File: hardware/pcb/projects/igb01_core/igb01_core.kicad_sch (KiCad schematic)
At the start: 65 parts, among them J1 STMP157_GPIO1, J10 BAT_CON, J11 VBUS_CON, J12 IGB2_NEXT, J13 IGB3_NEXT, J14 IGB4_NEXT, J15 I2C_PREV, J16 I2C_NEXT, J17 JTAG, J18 USB, J19 PWR_ON_CON, J2 STMP157_GPIO3, J20 FPA-VZA2-15-LF, J21 I2C2_NEXT, J3 STMP157_GPIO2, J4 STMP157_GPIO4, J5 STMP157_GPIO5, J6 STMP157_GPIO6, J7 LEFT_CON, J8 RIGHT_CON, J9 Micro_SD_Card, SW1 SW_DIP_x04, SW2 SW_Push, SW3 SW_Push, U1 W25Q128JVS

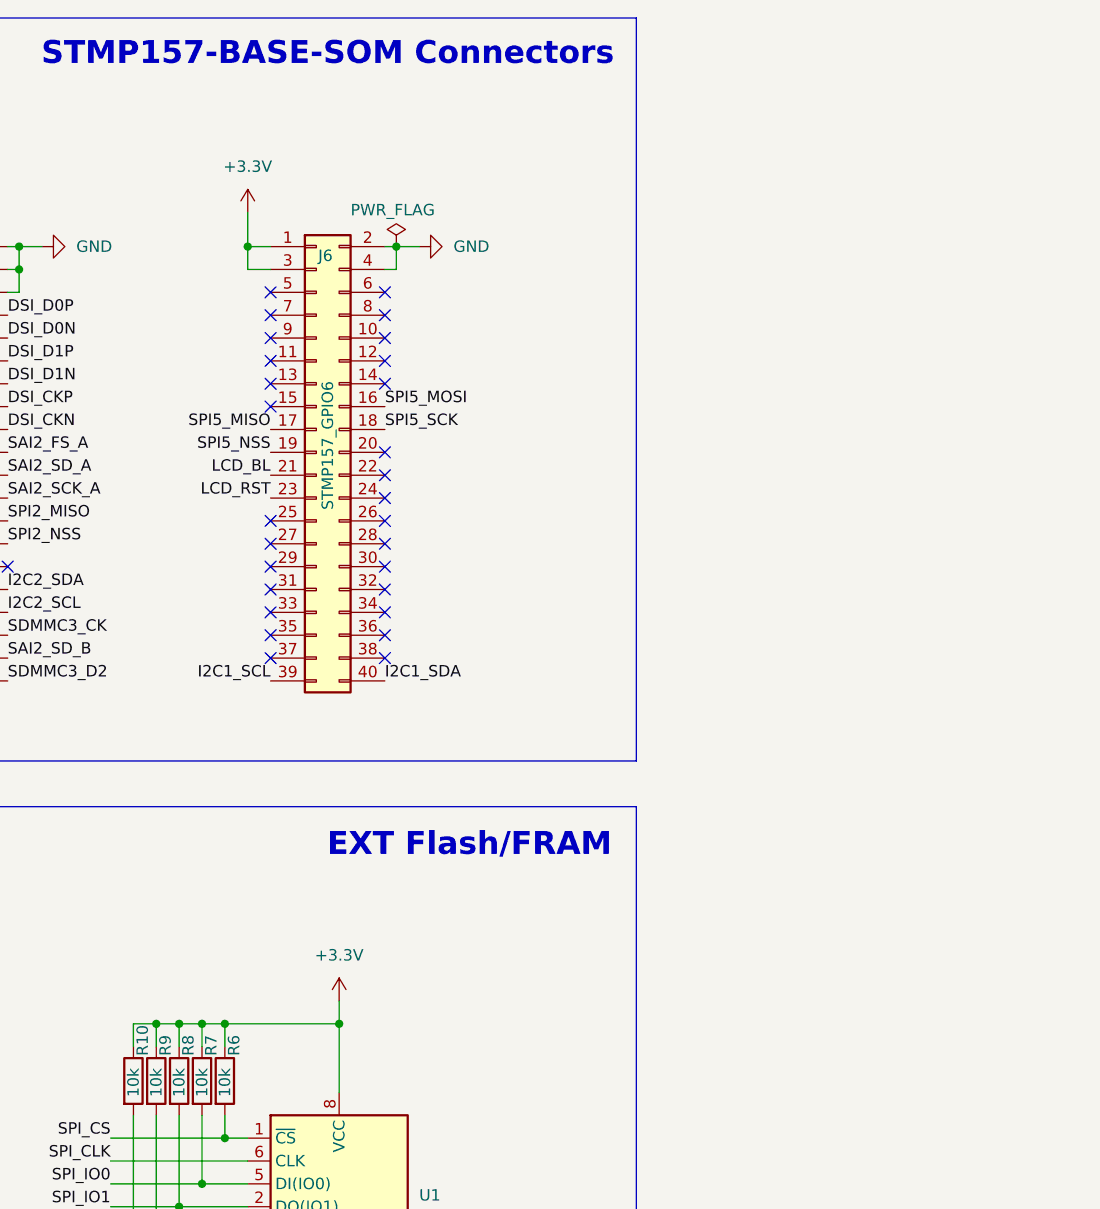
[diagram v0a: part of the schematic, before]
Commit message: add Config pins & Ext GPIO pins
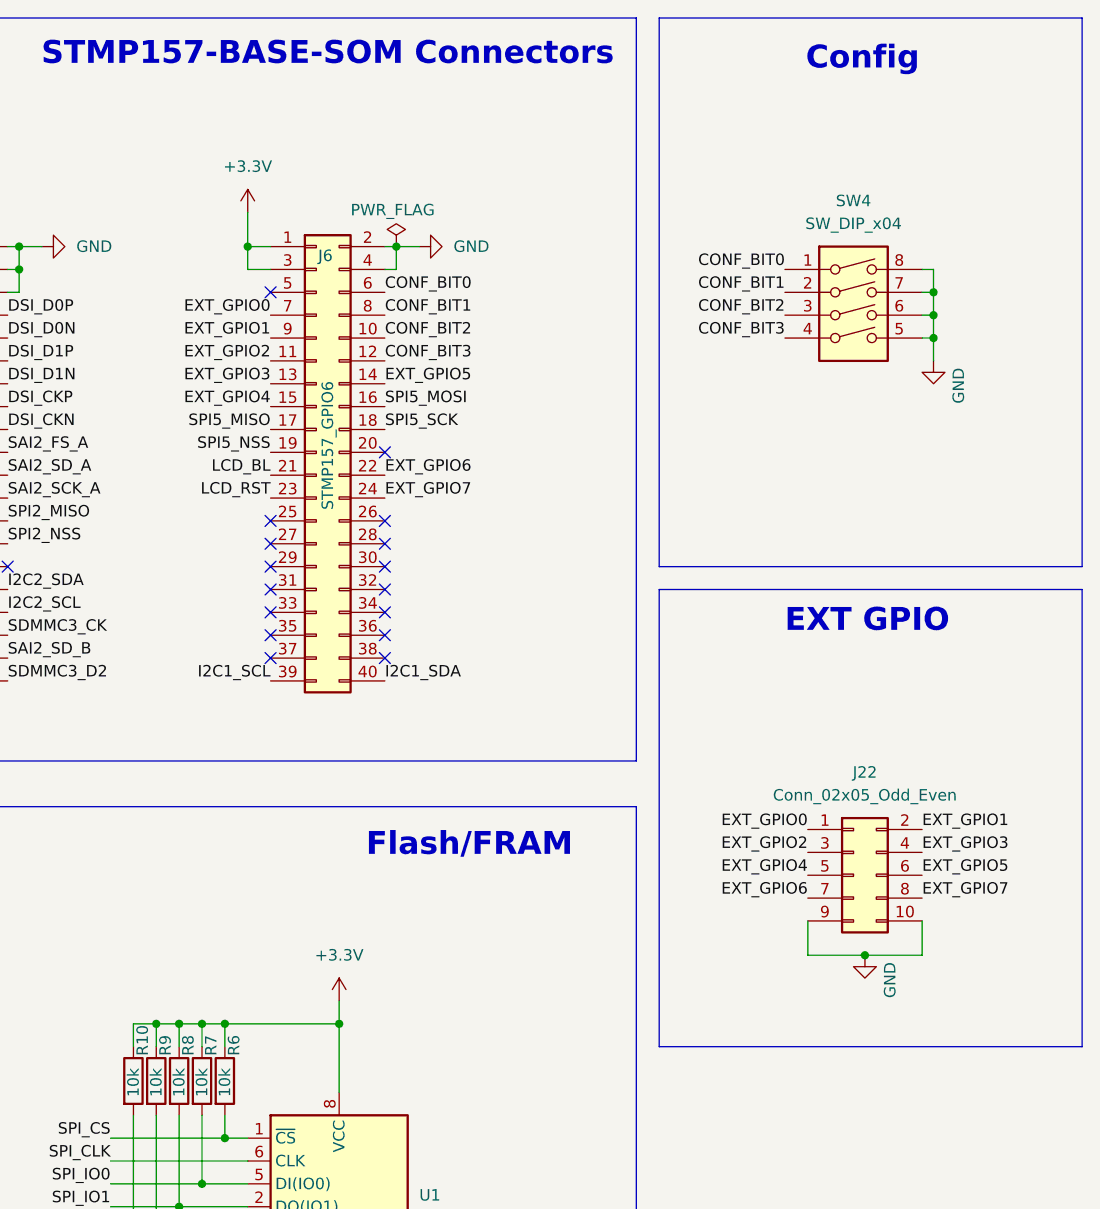
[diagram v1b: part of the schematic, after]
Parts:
- added J22: Conn_02x05_Odd_Even, symbol Connector_Generic:Conn_02x05_Odd_Even
- added SW4: SW_DIP_x04, symbol Switch:SW_DIP_x04
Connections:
- net GND: now also J22.10 (Pin_10), J22.9 (Pin_9), SW4.5, SW4.6, SW4.7, SW4.8
- net CONF_BIT2: now reaches J6.10 (Pin_10)
- net CONF_BIT2: now also SW4.3
- net EXT_GPIO2: now reaches J6.11 (Pin_11)
- net EXT_GPIO2: now also J22.3 (Pin_3)
- net CONF_BIT3: now reaches J6.12 (Pin_12)
- net CONF_BIT3: now also SW4.4
- net EXT_GPIO3: now reaches J6.13 (Pin_13)
- net EXT_GPIO3: now also J22.4 (Pin_4)
- net EXT_GPIO5: now reaches J6.14 (Pin_14)
- net EXT_GPIO5: now also J22.6 (Pin_6)
- net EXT_GPIO4: now reaches J6.15 (Pin_15)
- net EXT_GPIO4: now also J22.5 (Pin_5)
- net EXT_GPIO6: now reaches J6.22 (Pin_22)
- net EXT_GPIO6: now also J22.7 (Pin_7)
- net EXT_GPIO7: now reaches J6.24 (Pin_24)
- net EXT_GPIO7: now also J22.8 (Pin_8)
- net CONF_BIT0: now reaches J6.6 (Pin_6)
- net CONF_BIT0: now also SW4.1
- net EXT_GPIO0: now reaches J6.7 (Pin_7)
- net EXT_GPIO0: now also J22.1 (Pin_1)
- net CONF_BIT1: now reaches J6.8 (Pin_8)
- net CONF_BIT1: now also SW4.2
- net EXT_GPIO1: now reaches J6.9 (Pin_9)
- net EXT_GPIO1: now also J22.2 (Pin_2)
- no-connect marks 133 -> 121
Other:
- note added: "Config"
- note added: "EXT GPIO"
- note added: "Flash/FRAM"
- note removed: "EXT Flash/FRAM"

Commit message: add CODEC_PDN pin & 3.3V Out pin
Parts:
- J7, J8: symbol Connector_Generic:Conn_01x23 -> Connector_Generic:Conn_01x25
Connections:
- net +3.3V: now also J7.3 (Pin_3)
- net ADC1_INP1: now also J8.24 (Pin_24); no longer J7.3 (Pin_3)
- net ADC2_INP18: now also J8.25 (Pin_25); no longer J8.3 (Pin_3)
- net GND: now also J7.4 (Pin_4), J7.5 (Pin_5)
- net GPIO_CLOCK_OUT: now also J8.4 (Pin_4); no longer J8.5 (Pin_5)
- net GPIO_RESET_OUT: now also J8.3 (Pin_3); no longer J8.4 (Pin_4)
- net SDMMC3_CK: now also J7.24 (Pin_24); no longer J7.22 (Pin_22)
- net SDMMC3_CMD: now also J7.25 (Pin_25); no longer J7.23 (Pin_23)
- net SDMMC3_D0: now also J7.20 (Pin_20); no longer J7.18 (Pin_18)
- net SDMMC3_D1: now also J7.21 (Pin_21); no longer J7.19 (Pin_19)
- net SDMMC3_D2: now also J7.22 (Pin_22); no longer J7.20 (Pin_20)
- net SDMMC3_D3: now also J7.23 (Pin_23); no longer J7.21 (Pin_21)
- net SPI2_MISO: now also J7.14 (Pin_14); no longer J7.12 (Pin_12)
- net SPI2_MOSI: now also J7.13 (Pin_13); no longer J7.11 (Pin_11)
- net SPI2_NSS: now also J7.12 (Pin_12); no longer J7.10 (Pin_10)
- net SPI2_SCK: now also J7.15 (Pin_15); no longer J7.13 (Pin_13)
- net USART1_RX: now also J7.8 (Pin_8); no longer J7.6 (Pin_6)
- net USART1_TX: now also J7.9 (Pin_9); no longer J7.7 (Pin_7)
- net USART3_RX: now also J7.10 (Pin_10); no longer J7.8 (Pin_8)
- net USART3_TX: now also J7.11 (Pin_11); no longer J7.9 (Pin_9)
- net USART4_RX: now also J7.6 (Pin_6); no longer J7.4 (Pin_4)
- net USART4_TX: now also J7.7 (Pin_7); no longer J7.5 (Pin_5)
- net USB1_D+: now also J7.19 (Pin_19); no longer J7.17 (Pin_17)
- net USB1_D-: now also J7.18 (Pin_18); no longer J7.16 (Pin_16)
- net USB_OTG_FS_D+: now also J7.17 (Pin_17); no longer J7.15 (Pin_15)
- net USB_OTG_FS_D-: now also J7.16 (Pin_16); no longer J7.14 (Pin_14)
- net CODEC_PDN: now reaches J5.21 (Pin_21)
- net CODEC_PDN: now also J8.5 (Pin_5)
- no-connect marks 121 -> 120
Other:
- note added: "3.3VOut"
- note added: "5VIn"
- note added: "CV_IN"
- note removed: "CV1_IN"
- note removed: "CV2_IN"

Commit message: add LDC connectors on the core board
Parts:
- added C6, C7, C8: 47u, symbol Device:C_Small
- added J23: Conn_01x13, symbol Connector_Generic:Conn_01x13
- added J24: Conn_01x08, symbol Connector_Generic:Conn_01x08
- added R33, R34, R35, R36, R37, R38: 10k, symbol Device:R
- J7, J8: symbol Connector_Generic:Conn_01x25 -> Connector_Generic:Conn_01x23
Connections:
- net +3.3V: now also C6.1, C7.1, C8.2, J23.1 (Pin_1), J24.1 (Pin_1), R33.1, R34.1, R35.1, R36.1, R37.1, R38.1
- net ADC1_INP1: now also J8.22 (Pin_22); no longer J8.24 (Pin_24)
- net ADC2_INP18: now also J8.23 (Pin_23); no longer J8.25 (Pin_25)
- net CODEC_PDN: now also J8.3 (Pin_3); no longer J8.5 (Pin_5)
- net GND: now also J7.22 (Pin_22), J8.20 (Pin_20), C6.2, C7.2, C8.1, J23.2 (Pin_2), J24.2 (Pin_2)
- net GPIO_CLOCK_OUT: now also J7.23 (Pin_23); no longer J8.4 (Pin_4)
- net GPIO_RESET_OUT: now also J8.21 (Pin_21); no longer J8.3 (Pin_3)
- net I2C1_SCL: now also J8.10 (Pin_10); no longer J8.12 (Pin_12)
- net I2C1_SDA: now also J8.9 (Pin_9); no longer J8.11 (Pin_11)
- net I2C6_SCL: now also J23.11 (Pin_11)
- net I2C6_SDA: now also J23.10 (Pin_10)
- net LCD_BL: now also J23.9 (Pin_9), J24.8 (Pin_8), R37.2; no longer J8.18 (Pin_18)
- net LCD_RST: now also J23.8 (Pin_8), J24.7 (Pin_7), R36.2; no longer J8.19 (Pin_19)
- net SAI2_FS_A: now also J8.6 (Pin_6); no longer J8.8 (Pin_8)
- net SAI2_MCLK_A: now also J8.4 (Pin_4); no longer J8.6 (Pin_6)
- net SAI2_SCK_A: now also J8.5 (Pin_5); no longer J8.7 (Pin_7)
- net SAI2_SD_A: now also J8.7 (Pin_7); no longer J8.9 (Pin_9)
- net SAI2_SD_B: now also J8.8 (Pin_8); no longer J8.10 (Pin_10)
- net SDMMC3_CK: now also J7.20 (Pin_20); no longer J7.24 (Pin_24)
- net SDMMC3_CMD: now also J7.21 (Pin_21); no longer J7.25 (Pin_25)
- net SDMMC3_D0: now also J7.16 (Pin_16); no longer J7.20 (Pin_20)
- net SDMMC3_D1: now also J7.17 (Pin_17); no longer J7.21 (Pin_21)
- net SDMMC3_D2: now also J7.18 (Pin_18); no longer J7.22 (Pin_22)
- net SDMMC3_D3: now also J7.19 (Pin_19); no longer J7.23 (Pin_23)
- net SPI2_MISO: now also J8.18 (Pin_18); no longer J7.14 (Pin_14)
- net SPI2_MOSI: now also J8.17 (Pin_17); no longer J7.13 (Pin_13)
- net SPI2_NSS: now also J8.16 (Pin_16); no longer J7.12 (Pin_12)
- net SPI2_SCK: now also J8.19 (Pin_19); no longer J7.15 (Pin_15)
- net SPI4_GPIO_CS1: now also J8.11 (Pin_11); no longer J8.13 (Pin_13)
- net SPI4_MISO: now also J8.14 (Pin_14); no longer J8.16 (Pin_16)
- net SPI4_MOSI: now also J8.13 (Pin_13); no longer J8.15 (Pin_15)
- net SPI4_NSS: now also J8.12 (Pin_12); no longer J8.14 (Pin_14)
- net SPI4_SCK: now also J8.15 (Pin_15); no longer J8.17 (Pin_17)
- net SPI5_MISO: now also J23.3 (Pin_3), R35.2; no longer J8.22 (Pin_22)
- net SPI5_MOSI: now also J23.4 (Pin_4), J24.3 (Pin_3), R33.2; no longer J8.21 (Pin_21)
- net SPI5_NSS: now also J23.6 (Pin_6), J24.5 (Pin_5), R34.2; no longer J8.20 (Pin_20)
- net SPI5_SCK: now also J23.5 (Pin_5), J24.4 (Pin_4); no longer J8.23 (Pin_23)
- net USB1_D+: now also J7.15 (Pin_15); no longer J7.19 (Pin_19)
- net USB1_D-: now also J7.14 (Pin_14); no longer J7.18 (Pin_18)
- net USB_OTG_FS_D+: now also J7.13 (Pin_13); no longer J7.17 (Pin_17)
- net USB_OTG_FS_D-: now also J7.12 (Pin_12); no longer J7.16 (Pin_16)
- net LCD_DC: now reaches J6.20 (Pin_20)
- net LCD_DC: now also J23.7 (Pin_7), J24.6 (Pin_6), R38.2
- net LCD_TP_INT: now reaches J6.25 (Pin_25)
- net LCD_TP_INT: now also J23.12 (Pin_12)
- net LCD_TP_RST: now reaches J6.27 (Pin_27)
- net LCD_TP_RST: now also J23.13 (Pin_13)
- no-connect marks 120 -> 117
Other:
- note added: "Waveshare 1.28 LCD"
- note added: "Waveshare 1.28 LCD with Touch"
- note removed: "CLK_RST_OUT"
- note removed: "LCD_SPI (MISO=DC)"

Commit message: update core board
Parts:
- removed C6: 47u, symbol Device:C_Small
- removed J18: USB, symbol Connector_Generic:Conn_01x03
- removed J21: I2C2_NEXT, symbol Connector_Generic:Conn_01x03
- removed J22: Conn_02x05_Odd_Even, symbol Connector_Generic:Conn_02x05_Odd_Even
- removed J24: Conn_01x08, symbol Connector_Generic:Conn_01x08
- removed R23, R24, R31, R32: 47, symbol Device:R
- removed SW4: SW_DIP_x04, symbol Switch:SW_DIP_x04
- added C10, C11, C12, C20, C21, C22, C23, C9: 1u_SMD, Capacitor_SMD:C_1206_3216Metric, symbol Device:C_Small
- added C13, C17: 2.2u, Capacitor_SMD:C_0603_1608Metric, symbol Device:C_Small
- added C14, C18, C8: 100n, Capacitor_SMD:C_0402_1005Metric, symbol Device:C_Small
- added C15, C19, C7: 22u, Capacitor_SMD:C_0805_2012Metric, symbol Device:C_Small
- added J14: USB_CONN, Connector_Molex:Molex_KK-254_AE-6410-06A_1x06_P2.54mm_Vertical, symbol Connector_Generic:Conn_01x06
- added R35, R36, R37, R42, R43, R44, R45, R46: 22, Resistor_SMD:R_0402_1005Metric, symbol Device:R
- added R38, R39, R40, R41: 0, Resistor_SMD:R_0603_1608Metric, symbol Device:R
- added R47, R48: 10k, Resistor_SMD:R_0603_1608Metric, symbol Device:R
- added U2: AK4619, Package_DFN_QFN:QFN-32-1EP_5x5mm_P0.5mm_EP3.6x3.6mm, symbol AK4619:AK4619
- C1: footprint (none) -> Resistor_SMD:R_1206_3216Metric
- C16: renamed from C7; footprint (none) -> Resistor_SMD:R_1206_3216Metric
- C2: renamed from C4; footprint (none) -> Resistor_SMD:R_1206_3216Metric
- C3: renamed from C5; footprint (none) -> Resistor_SMD:R_1206_3216Metric
- C4: renamed from C2; footprint (none) -> Resistor_SMD:R_1206_3216Metric
- C5: renamed from C3; footprint (none) -> Resistor_SMD:R_0603_1608Metric
- C6: renamed from C8; footprint (none) -> Resistor_SMD:R_1206_3216Metric
- J1: footprint (none) -> Connector_PinHeader_1.27mm:PinHeader_2x20_P1.27mm_Vertical_SMD
- J10: renamed from J15; footprint (none) -> Connector_Molex:Molex_KK-254_AE-6410-03A_1x03_P2.54mm_Vertical
- J11: renamed from J16; footprint (none) -> Connector_Molex:Molex_KK-254_AE-6410-03A_1x03_P2.54mm_Vertical
- J12: renamed from J2; footprint (none) -> Connector_PinHeader_1.27mm:PinHeader_2x20_P1.27mm_Vertical_SMD
- J13: renamed from J17; footprint (none) -> Connector_PinHeader_1.27mm:PinHeader_2x05_P1.27mm_Vertical_SMD
- J15: renamed from J4; footprint (none) -> Connector_PinHeader_1.27mm:PinHeader_2x20_P1.27mm_Vertical_SMD
- J16: renamed from J9; footprint (none) -> kicadlib:Molex_uSD_1040310811
- J17: renamed from J19; footprint (none) -> Connector_PinHeader_2.54mm:PinHeader_1x01_P2.54mm_Vertical
- J18: renamed from J5; footprint (none) -> Connector_PinHeader_1.27mm:PinHeader_2x20_P1.27mm_Vertical_SMD
- J19: renamed from J6; footprint (none) -> Connector_PinHeader_1.27mm:PinHeader_2x20_P1.27mm_Vertical_SMD
- J2: renamed from J10; footprint (none) -> Connector_Molex:Molex_KK-254_AE-6410-02A_1x02_P2.54mm_Vertical
- J20: footprint (none) -> Connector_FFC-FPC:Molex_200528-0150_1x15-1MP_P1.00mm_Horizontal; symbol Connector_Generic:Conn_02x15_Counter_Clockwise -> Connector_Generic_MountingPin:Conn_01x15_MountingPin
- J22: renamed from J23; footprint (none) -> Connector_PinHeader_2.54mm:PinHeader_1x13_P2.54mm_Horizontal
- J3: renamed from J11; footprint (none) -> Connector_Molex:Molex_KK-254_AE-6410-02A_1x02_P2.54mm_Vertical
- J4: renamed from J7; footprint (none) -> Connector_PinHeader_2.54mm:PinHeader_1x23_P2.54mm_Vertical
- J5: renamed from J8; footprint (none) -> Connector_PinHeader_2.54mm:PinHeader_1x23_P2.54mm_Vertical
- J6: renamed from J3; footprint (none) -> Connector_PinHeader_1.27mm:PinHeader_2x20_P1.27mm_Vertical_SMD
- J7: renamed from J12; footprint (none) -> Connector_Molex:Molex_KK-254_AE-6410-03A_1x03_P2.54mm_Vertical
- J8: renamed from J13; footprint (none) -> Connector_Molex:Molex_KK-254_AE-6410-03A_1x03_P2.54mm_Vertical
- J9: renamed from J14; footprint (none) -> Connector_Molex:Molex_KK-254_AE-6410-03A_1x03_P2.54mm_Vertical
- R1: renamed from R11; footprint (none) -> Resistor_SMD:R_0603_1608Metric
- R10: renamed from R20; footprint (none) -> Resistor_SMD:R_0603_1608Metric
- R11: renamed from R21; footprint (none) -> Resistor_SMD:R_0603_1608Metric
- R12: renamed from R5; footprint (none) -> Resistor_SMD:R_0603_1608Metric
- R13: renamed from R4; footprint (none) -> Resistor_SMD:R_0603_1608Metric
- R14: renamed from R3; footprint (none) -> Resistor_SMD:R_0603_1608Metric
- R15: renamed from R2; footprint (none) -> Resistor_SMD:R_0603_1608Metric
- R16: renamed from R22; footprint (none) -> Resistor_SMD:R_0603_1608Metric
- R17: renamed from R1; footprint (none) -> Resistor_SMD:R_0603_1608Metric
- R18: renamed from R25; footprint (none) -> Resistor_SMD:R_0603_1608Metric
- R19: renamed from R26; footprint (none) -> Resistor_SMD:R_0603_1608Metric
- R2: renamed from R12; footprint (none) -> Resistor_SMD:R_0603_1608Metric
- R20: renamed from R10; footprint (none) -> Resistor_SMD:R_0603_1608Metric
- R21: renamed from R9; footprint (none) -> Resistor_SMD:R_0603_1608Metric
- R22: renamed from R27; footprint (none) -> Resistor_SMD:R_0603_1608Metric
- R23: renamed from R8; footprint (none) -> Resistor_SMD:R_0603_1608Metric
- R24: renamed from R7; footprint (none) -> Resistor_SMD:R_0603_1608Metric
- R25: renamed from R28; footprint (none) -> Resistor_SMD:R_0603_1608Metric
- R26: renamed from R6; footprint (none) -> Resistor_SMD:R_0603_1608Metric
- R27: renamed from R29; footprint (none) -> Resistor_SMD:R_0603_1608Metric
- R28: renamed from R30; footprint (none) -> Resistor_SMD:R_0603_1608Metric
- R29: renamed from R33; footprint (none) -> Resistor_SMD:R_0603_1608Metric
- R3: renamed from R13; footprint (none) -> Resistor_SMD:R_0603_1608Metric
- R30: renamed from R34; footprint (none) -> Resistor_SMD:R_0603_1608Metric
- R31: renamed from R35; footprint (none) -> Resistor_SMD:R_0603_1608Metric
- R32: renamed from R36; footprint (none) -> Resistor_SMD:R_0603_1608Metric
- R33: renamed from R37; footprint (none) -> Resistor_SMD:R_0603_1608Metric
- R34: renamed from R38; footprint (none) -> Resistor_SMD:R_0603_1608Metric
- R4: renamed from R14; footprint (none) -> Resistor_SMD:R_0603_1608Metric
- R5: renamed from R15; footprint (none) -> Resistor_SMD:R_0603_1608Metric
- R6: renamed from R16; footprint (none) -> Resistor_SMD:R_0603_1608Metric
- R7: renamed from R17; footprint (none) -> Resistor_SMD:R_0603_1608Metric
- R8: renamed from R18; footprint (none) -> Resistor_SMD:R_0603_1608Metric
- R9: renamed from R19; footprint (none) -> Resistor_SMD:R_0603_1608Metric
- SW1: footprint (none) -> Package_DIP:SMDIP-8_W9.53mm
- SW2, SW3: footprint (none) -> Button_Switch_SMD:SW_SPST_PTS647_Sx38
- TP1, TP2, TP3: footprint (none) -> Connector_PinHeader_2.54mm:PinHeader_1x01_P2.54mm_Vertical
- U1: footprint Package_SO:SOIC-8_5.23x5.23mm_P1.27mm -> Package_SO:SOIC-8_5.3x5.3mm_P1.27mm
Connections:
- net +3.3V: now also C7.1, C8.1, R47.2, R48.2, U2.3 (TVDD)
- net +5V: now also J14.3 (Pin_3)
- net ADC1_INP1: now also J5.12 (Pin_12); no longer J5.22 (Pin_22)
- net ADC2_INP18: now also J5.13 (Pin_13); no longer J5.23 (Pin_23)
- net CODEC_PDN: now also R46.2; no longer J5.3 (Pin_3)
- net CONF_BIT0: now also R38.1
- net CONF_BIT1: now also R39.1
- net CONF_BIT2: now also R40.1
- net CONF_BIT3: now also R41.1
- net GND: now also J20.MP (MountPin), J4.12 (Pin_12), J4.23 (Pin_23), J5.14 (Pin_14), C13.2, C7.2, C8.2, J14.4 (Pin_4), R38.2, R39.2, R40.2, R41.2, U2.2 (SDIN2), U2.27 (I2CAD/CS), U2.4 (VSS2); no longer J4.22 (Pin_22), J5.1 (Pin_1), J5.2 (Pin_2), J5.20 (Pin_20)
- net GPIO_CLOCK_OUT: now also J5.22 (Pin_22); no longer J4.23 (Pin_23)
- net GPIO_RESET_OUT: now also J5.23 (Pin_23); no longer J5.21 (Pin_21)
- net I2C1_SCL: now also J5.16 (Pin_16); no longer J5.10 (Pin_10)
- net I2C1_SDA: now also J5.15 (Pin_15); no longer J5.9 (Pin_9)
- net I2C2_SCL: now also R45.2, R47.1; no longer R8.2
- net I2C2_SDA: now also R44.2, R48.1; no longer R9.2
- net I2C3_SCL: now also R8.2; no longer R10.2
- net I2C3_SDA: now also R9.2; no longer R11.2
- net I2C4_SCL: now also R10.2
- net I2C4_SDA: now also R11.2
- net SAI2_FS_A: now also R35.1; no longer J5.6 (Pin_6)
- net SAI2_MCLK_A: now also R37.1; no longer J5.4 (Pin_4)
- net SAI2_SCK_A: now also R36.1; no longer J5.5 (Pin_5)
- net SAI2_SD_A: now also R43.2; no longer J5.7 (Pin_7)
- net SAI2_SD_B: now also R42.1; no longer J5.8 (Pin_8)
- net SDMMC3_CK: now also J4.17 (Pin_17); no longer J4.20 (Pin_20)
- net SDMMC3_CMD: now also J4.18 (Pin_18); no longer J4.21 (Pin_21)
- net SDMMC3_D0: now also J4.13 (Pin_13); no longer J4.16 (Pin_16)
- net SDMMC3_D1: now also J4.14 (Pin_14); no longer J4.17 (Pin_17)
- net SDMMC3_D2: now also J4.15 (Pin_15); no longer J4.18 (Pin_18)
- net SDMMC3_D3: now also J4.16 (Pin_16); no longer J4.19 (Pin_19)
- net SPI2_MISO: now also J4.21 (Pin_21); no longer J5.18 (Pin_18)
- net SPI2_MOSI: now also J4.20 (Pin_20); no longer J5.17 (Pin_17)
- net SPI2_NSS: now also J4.19 (Pin_19); no longer J5.16 (Pin_16)
- net SPI2_SCK: now also J4.22 (Pin_22); no longer J5.19 (Pin_19)
- net SPI4_GPIO_CS1: now also J5.17 (Pin_17); no longer J5.11 (Pin_11)
- net SPI4_MISO: now also J5.20 (Pin_20); no longer J5.14 (Pin_14)
- net SPI4_MOSI: now also J5.19 (Pin_19); no longer J5.13 (Pin_13)
- net SPI4_NSS: now also J5.18 (Pin_18); no longer J5.12 (Pin_12)
- net SPI4_SCK: now also J5.21 (Pin_21); no longer J5.15 (Pin_15)
- net USB1_D+: now also J14.1 (Pin_1); no longer J4.15 (Pin_15)
- net USB1_D-: now also J14.2 (Pin_2); no longer J4.14 (Pin_14)
- net USB_OTG_FS_D+: now also J14.5 (Pin_5); no longer J4.13 (Pin_13)
- net USB_OTG_FS_D-: now also J14.6 (Pin_6); no longer J4.12 (Pin_12)
- net USB2_D+: no longer names the net of J6.27 (Pin_27)
- net USB2_D-: no longer names the net of J6.25 (Pin_25)
- new net: C23.1, U2.22 (AOUT1L)
- new net: R36.2, U2.7 (BICK)
- new net: C18.1, C19.1, U2.21 (VREFH)
- new net: C21.1, U2.24 (AOUT2L)
- new net: R42.2, U2.1 (SDIN1)
- new net: C9.2, U2.10 (IN4P)
- new net: C10.2, U2.12 (IN3P)
- new net: C11.2, U2.14 (IN2P)
- new net: C12.2, U2.16 (IN1P)
- new net: C17.1, U2.17 (VCOM)
- new net: C22.1, U2.23 (AOUT1R)
- new net: C20.1, U2.25 (AOUT2R)
- new net: R46.1, U2.26 (PDN)
- new net: R45.1, U2.28 (SCL/SCLK)
- new net: R44.1, U2.30 (SDA/MISO)
- new net: R43.1, U2.31 (SDOUT1)
- new net: C13.1, U2.5 (AVDRV)
- new net: R35.2, U2.6 (LRCK)
- new net: R37.2, U2.8 (MCLK)
- new net +3.3VA: C14.1, C15.1, J5.1 (Pin_1), U2.18 (AVDD)
- new net GNDA: C14.2, C15.2, C17.2, C18.2, C19.2, J5.2 (Pin_2), J5.7 (Pin_7), U2.19 (VSS1), U2.20 (VREFL), U2.33 (EP)
- new net IN1L: C12.1, J5.3 (Pin_3)
- new net IN1R: C11.1, J5.4 (Pin_4)
- new net IN2L: C10.1, J5.5 (Pin_5)
- new net IN2R: C9.1, J5.6 (Pin_6)
- new net OUT1L: C23.2, J5.8 (Pin_8)
- new net OUT1R: C22.2, J5.9 (Pin_9)
- new net OUT2L: C21.2, J5.10 (Pin_10)
- new net OUT2R: C20.2, J5.11 (Pin_11)
- no-connect marks 117 -> 110
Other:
- note added: "ANALOG IN"
- note added: "ANALOG OUT"
- note added: "CODEC"
- note added: "DEVICE"
- note added: "HOST"
- note added: "Single-Ended Input"
- note added: "TDM Mode"
- note removed: "CODEC_SAI"
- note removed: "EXT GPIO"
- note removed: "USB_DEVICE"
- note removed: "USB_HOST"
- note removed: "Waveshare 1.28 LCD"
- moved on the sheet: C16, C6, J22, R18, R19, R20, R21, R22, R23, R24, R25, R26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
